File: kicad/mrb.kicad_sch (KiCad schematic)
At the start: 8 parts

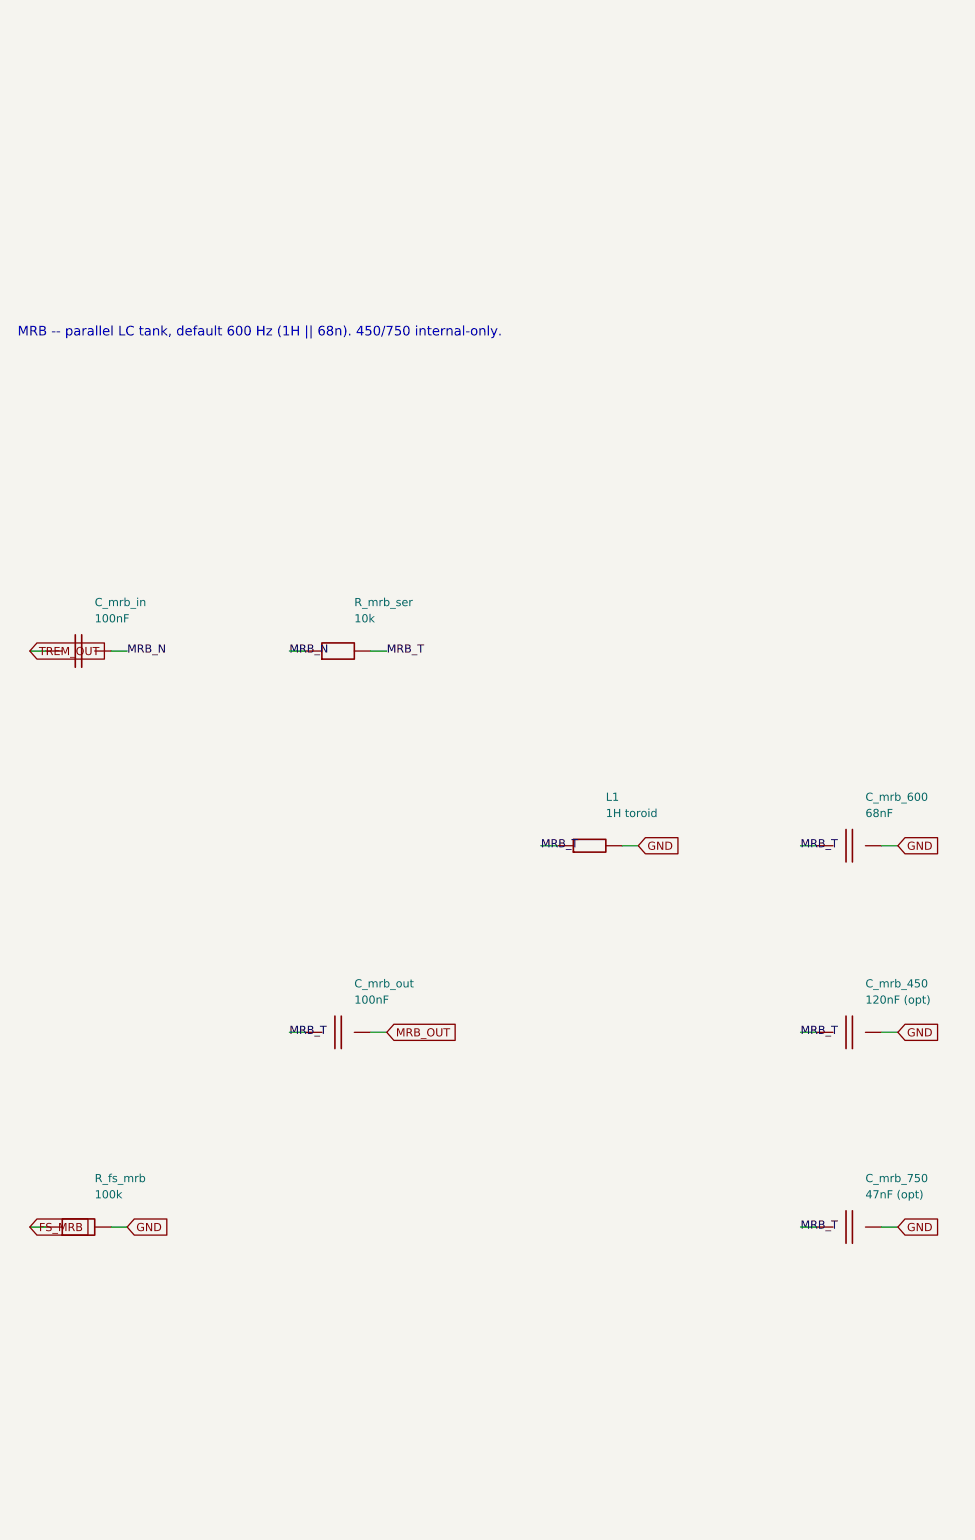
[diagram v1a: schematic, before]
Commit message: Add 26 labelled bench test points (schematic + BOM + silk) and re-route
Test points follow the Part 5 bring-up order: rails (VRAW, +33V5, VREG_IN,
+17V), JFET drains Q1D/Q2D/QRD (the errata #15 bias trim), the VBIAS_R/VBIAS_T
mid-rail refs, every inter-stage node (PREAMP_OUT, TONE_OUT, BLEND, TREM_OUT,
MRB_OUT, PA_IN), tank drive/return, LFO, PA_BIAS/PA_OUT/SPK_P, and a GND pin
per zone for the probe clip.

- gen_kicad.py: one-pin TP symbol; TEST_POINTS table; add_test_points() puts
  them on their sheets so they are in the netlist and the BOM (one order line)
- footprint TestPoint_THT_D2.0mm_Label: 2.0 mm pad / 1.0 mm drill for a header
  pin or wire loop; the footprint VALUE (= net alias) prints on F.SilkS
- gen_pcb.py: test-point strip across the top of each zone; the effects column
  is now two stacked zones (tremolo+MRB above, reverb below next to its tank
  pads) so each block's points sit right above its parts; stacked-zone gap 2 mm
- PCB-NOTES.md: test-point table with expected values (Part 3 troubleshooting,
  Part 2 set-up, ngspice) and the bring-up sequence
- Re-routed (Freerouting 1.9.0, B.Cu x7, via 60): 161/166 connections, 0 DRC
  violations, 54 vias; the five open links are listed for a GUI finish

Co-Authored-By: Claude Fable 5.1 <noreply@anthropic.com>
Claude-Session: https://claude.ai/code/session_01Vk8HkvCugxFpQsBPVnNT2H
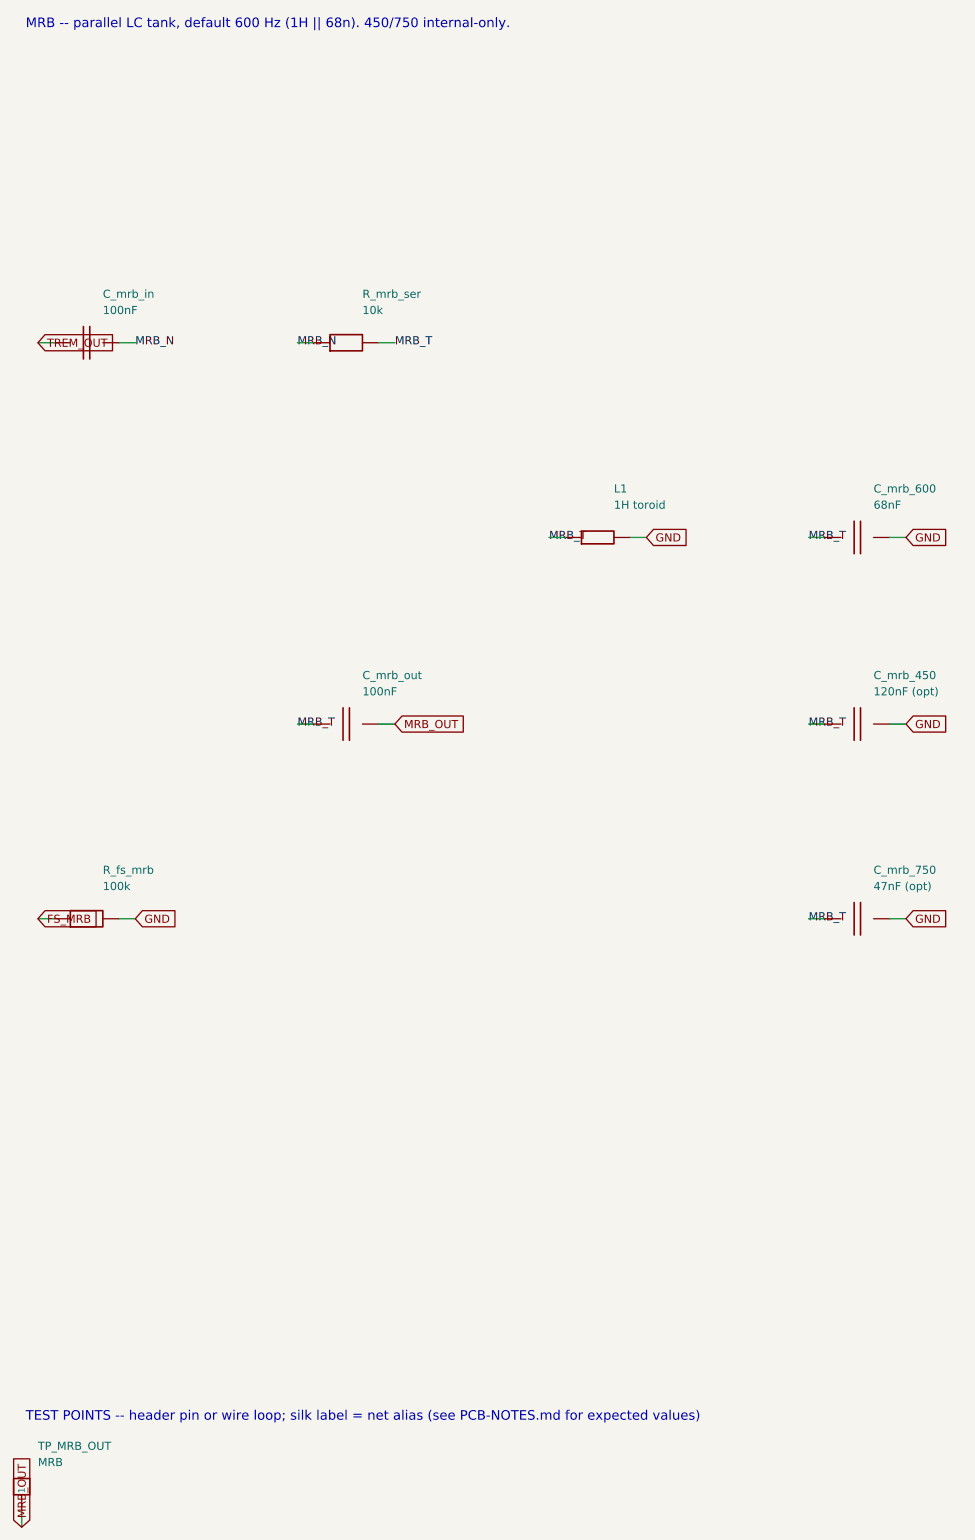
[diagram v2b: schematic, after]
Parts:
- added TP_MRB_OUT: MRB, cambridge_reverb:TestPoint_THT_D2.0mm_Label, symbol cr_primitives:TP
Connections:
- net MRB_OUT: now also TP_MRB_OUT.1
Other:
- note added: "TEST POINTS -- header pin or wire loop; silk label = net alias (see PCB-NOTES.md for expected values)"
